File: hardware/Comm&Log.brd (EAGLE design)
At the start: 47 x 40.5 mm, 25 parts, among them J1 DM3AT-SF-PEJM5, U1 S25FL116K0XMFI043, U2 CAT24M01

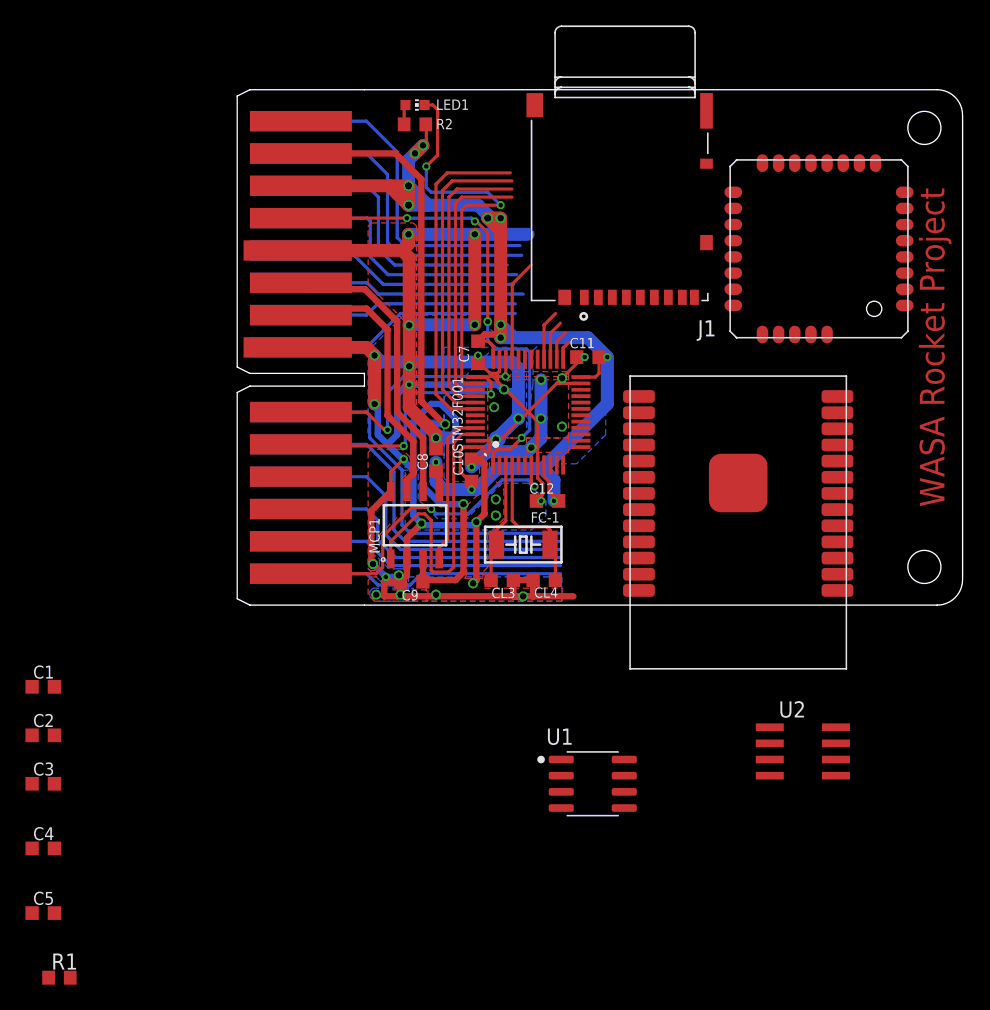
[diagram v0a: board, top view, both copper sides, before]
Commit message: Complete communication & logging board
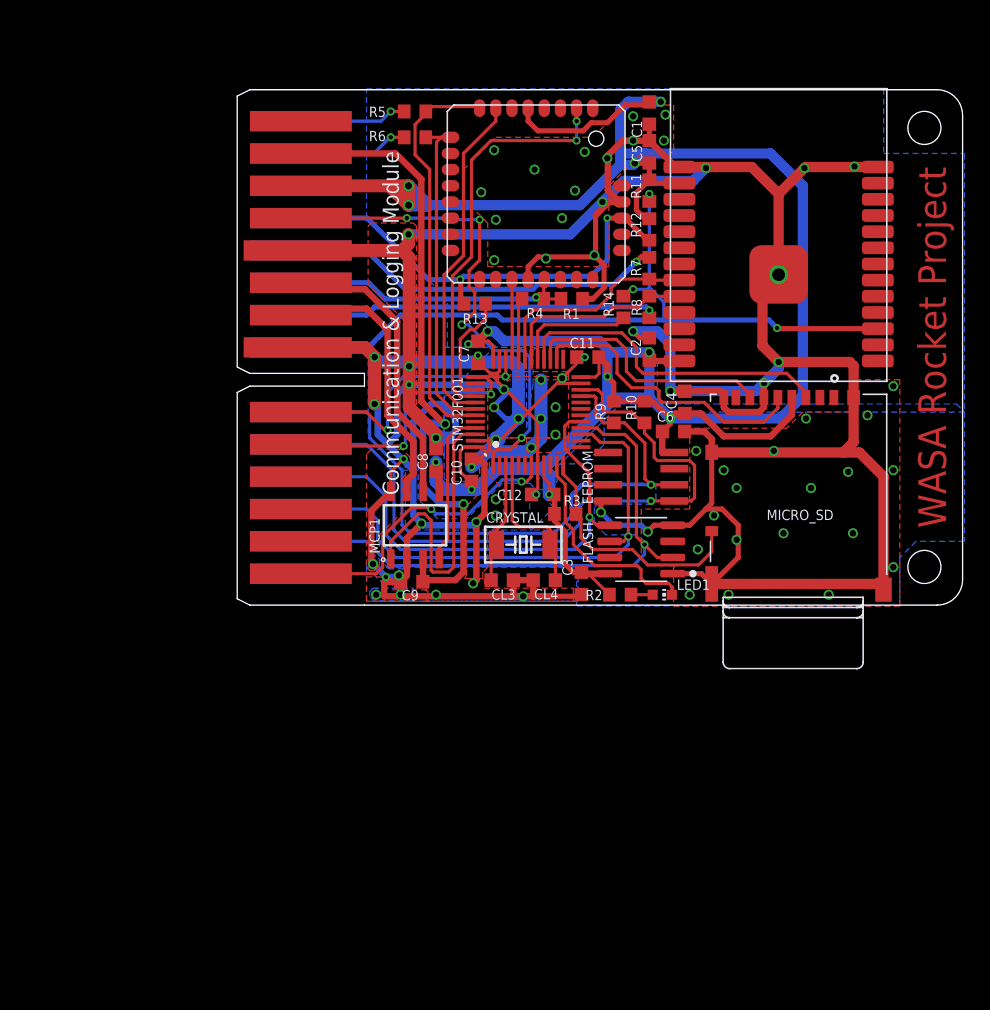
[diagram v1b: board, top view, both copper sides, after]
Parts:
- removed J1: DM3AT-SF-PEJM5, dm3at-sf-pejm5:HRS_DM3AT-SF-PEJM5
- removed U$1: ES920LR, FaBo-LoRa:ES920LR
- removed U$3: LITE, TWELite:LITE
- removed U1: S25FL116K0XMFI043, S25FL116K0XMFI043:SOIC127P600X175-8N
- removed U2: CAT24M01, CAT24M01:SO-8
- added C6: 0.1µF, rcl:C0603K
- added EEPROM: CAT24M01, CAT24M01:SO-8
- added ES920LR: ES920LR, FaBo-LoRa:ES920LR
- added FLASH: S25FL116K0XMFI043, S25FL116K0XMFI043:SOIC127P600X175-8N
- added MICRO_SD: DM3AT-SF-PEJM5, dm3at-sf-pejm5:HRS_DM3AT-SF-PEJM5
- added R10, R11, R12, R9: 10k, resistor:R0603
- added R13, R14: 1k, resistor:R0603
- added R3: 10k, rcl:R0603
- added R4, R5, R6, R7, R8: 1k, rcl:R0603
- added TWE-LITE: LITE, TWELite:LITE
- moved C5 76.5 mm to (32.4, 15.4), turned to 270 degrees
- moved R1 66.8 mm to (26.3, 3.81), turned to 180 degrees
- moved C1 65.6 mm to (32.4, 18.4), turned to 270 degrees
- moved C4 61.4 mm to (35.2, -4.32), turned to 90 degrees
- moved C2 56.5 mm to (32.4, -0.13), turned to 90 degrees
- moved C3 45.1 mm to (27.1, -18.5), turned to 270 degrees
- moved LED1 43.1 mm to (33.4, -19.4)
- moved R2 40.3 mm to (30.1, -19.4), turned to 0 degrees
- moved C12 0.63 mm to (24.0, -11.6)
- renumbered FC-1 to CRYSTAL
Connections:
- removed net 920_USART_RX: STM32F001.31, U$1.8
- removed net 920_USART_TX: STM32F001.30, U$1.9
- removed net I2C1_SCL: STM32F001.42, U2.6
- removed net I2C1_SDA: STM32F001.43, U2.5
- removed net N$33: U$2.30
- removed net N$34: U$2.29
- removed net N$35: U$2.28
- removed net N$36: U$2.27
- removed net N$43: U$2.26
- removed net N$44: U$2.25
- removed net N$45: U$2.23
- removed net N$46: U$2.22
- removed net N$47: U$2.21
- removed net N$48: U$2.20
- removed net N$49: U$2.19
- removed net N$50: U$2.18
- removed net N$56: STM32F001.15
- removed net N$57: STM32F001.16
- removed net N$58: STM32F001.17
- removed net N$61: STM32F001.33
- removed net N$65: STM32F001.21
- removed net N$66: J1.SWA, STM32F001.22
- removed net SPI1_MISO: J1.7, STM32F001.40
- removed net SPI1_MOSI: J1.3, STM32F001.41
- removed net SPI1_NSS: J1.2, STM32F001.38
- removed net SPI1_SCK: J1.5, STM32F001.39
- removed net SPI2_MISO: STM32F001.27, U1.2
- removed net SPI2_MOSI: STM32F001.28, U1.5
- removed net SPI2_NSS: STM32F001.25, U1.1
- removed net SPI2_SCK: STM32F001.26, U1.6
- removed net TWE_USART_RX: STM32F001.13, U$3.8
- removed net TWE_USART_TX: STM32F001.12, U$3.9
- new net 920_!SLEEP!': R14.1, STM32F001.29
- new net 920_RTX: ES920LR.8, R7.1, STM32F001.31
- new net 920_TRX: ES920LR.9, R8.1, STM32F001.30
- new net EEPROM_SCL: EEPROM.6, R9.1, STM32F001.21, U$2.25
- new net EEPROM_SDA: EEPROM.5, R10.1, STM32F001.22, U$2.26
- new net FLASH_MISO: FLASH.2, STM32F001.16, U$2.29
- new net FLASH_MOSI: FLASH.5, STM32F001.17, U$2.27
- new net FLASH_SCK: FLASH.6, STM32F001.15, U$2.28
- new net N$1: ES920LR.24
- new net N$3: R4.1, STM32F001.32
- new net N$4: R6.2, U$2.17
- new net N$5: R7.2, U$2.20
- new net N$6: R13.1, STM32F001.39
- new net SD_!SS!: MICRO_SD.2
- new net SD_!SW!: MICRO_SD.SWA, R3.2, STM32F001.12
- new net SD_MISO: MICRO_SD.7, STM32F001.27
- new net SD_MOSI: MICRO_SD.3, STM32F001.28
- new net SD_SCK: MICRO_SD.5, STM32F001.26
- new net TWE_BPS: STM32F001.33, TWE-LITE.19
- new net TWE_RTX: R5.1, STM32F001.43, TWE-LITE.8
- new net TWE_TRX: R6.1, STM32F001.42, TWE-LITE.9
- net 920_!SLEEP!: now also ES920LR.16, R11.1, R14.2, U$2.23; no longer U$1.16
- net GND: now also C6.2, EEPROM.4, ES920LR.1, ES920LR.26, ES920LR.GND, FLASH.1, FLASH.4, MICRO_SD.6, MICRO_SD.P1, MICRO_SD.P2, MICRO_SD.P3, MICRO_SD.P4, MICRO_SD.SWB, R1.1, TWE-LITE.20, TWE-LITE.28; no longer J1.6, J1.P1, J1.P2, J1.P3, J1.P4, J1.SWB, U$1.1, U$1.26, U$1.GND, U$3.20, U$3.28, U1.4, U2.4
- net N$2: now also R8.2, U$2.22; no longer U2.2
- net N$73: now also STM32F001.11
- net N$74: now also R5.2
- net TWE_!PGM!: now also STM32F001.40, TWE-LITE.2; no longer STM32F001.10, U$3.2
- net TWE_!RESET!: now also R1.2, R4.2, TWE-LITE.21, U$2.21; no longer R1.1, STM32F001.14, U$3.21
- net TWE_!RTS!: now also STM32F001.41, TWE-LITE.7; no longer STM32F001.11, U$3.7
- net TWE_SLEEP: now also R12.1, R13.2, TWE-LITE.27, U$2.19; no longer U$2.17, U$3.27
- net VDD: now also C6.1, EEPROM.8, ES920LR.13, ES920LR.2, FLASH.8, MICRO_SD.4, R10.2, R11.2, R12.2, R3.1, R9.2, TWE-LITE.5; no longer J1.4, R1.2, U$1.13, U$1.2, U$3.5, U1.8, U2.8
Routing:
- net GND: track 217.6 -> 396.7 mm, vias 35 -> 78
- net VDD: track 96.7 -> 214.9 mm
- net 920_!SLEEP!: track 0.00 -> 60.2 mm, vias 0 -> 3
- net EEPROM_SDA: track 0.00 -> 54.8 mm, vias 0 -> 1
- net EEPROM_SCL: track 0.00 -> 50.2 mm, vias 0 -> 1
- net FLASH_MISO: track 0.00 -> 44.5 mm, vias 0 -> 1
- net FLASH_SCK: track 0.00 -> 42.0 mm, vias 0 -> 1
- net FLASH_MOSI: track 0.00 -> 40.0 mm, vias 0 -> 1
- net TWE_!PGM!: track 0.00 -> 32.0 mm, vias 0 -> 2
- net TWE_RTX: track 0.00 -> 31.9 mm
- net N$5: track 0.00 -> 29.7 mm, vias 0 -> 1
- net N$2: track 0.00 -> 28.3 mm, vias 0 -> 1
- net N$44: track 27.8 -> 0.00 mm
- net TWE_!RTS!: track 0.00 -> 26.7 mm
- net TWE_TRX: track 0.00 -> 26.5 mm
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- added copper zone on layer 16, net VDD
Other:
- board text added: "Communication & Logging Module"
- board text added: "Designed by @fujiy0, 2019"

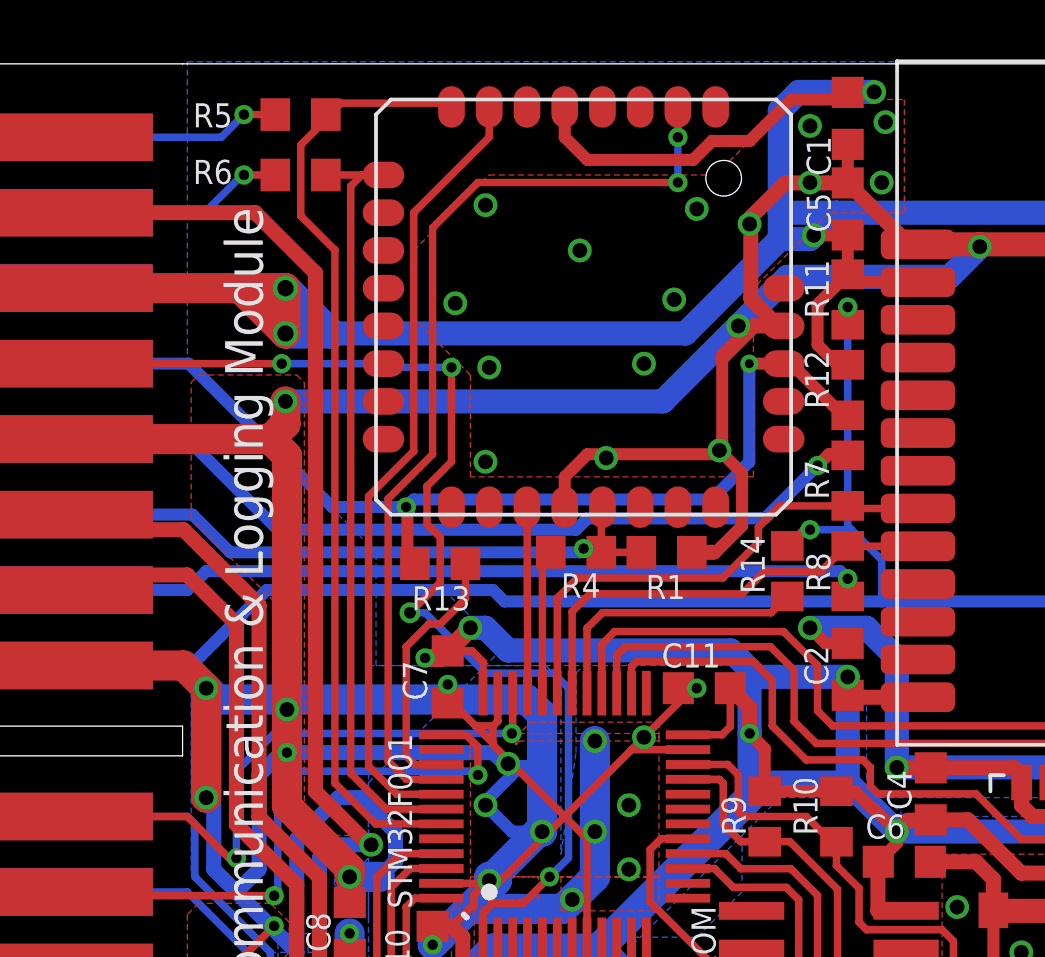
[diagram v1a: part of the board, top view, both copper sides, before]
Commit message: Clean silk print
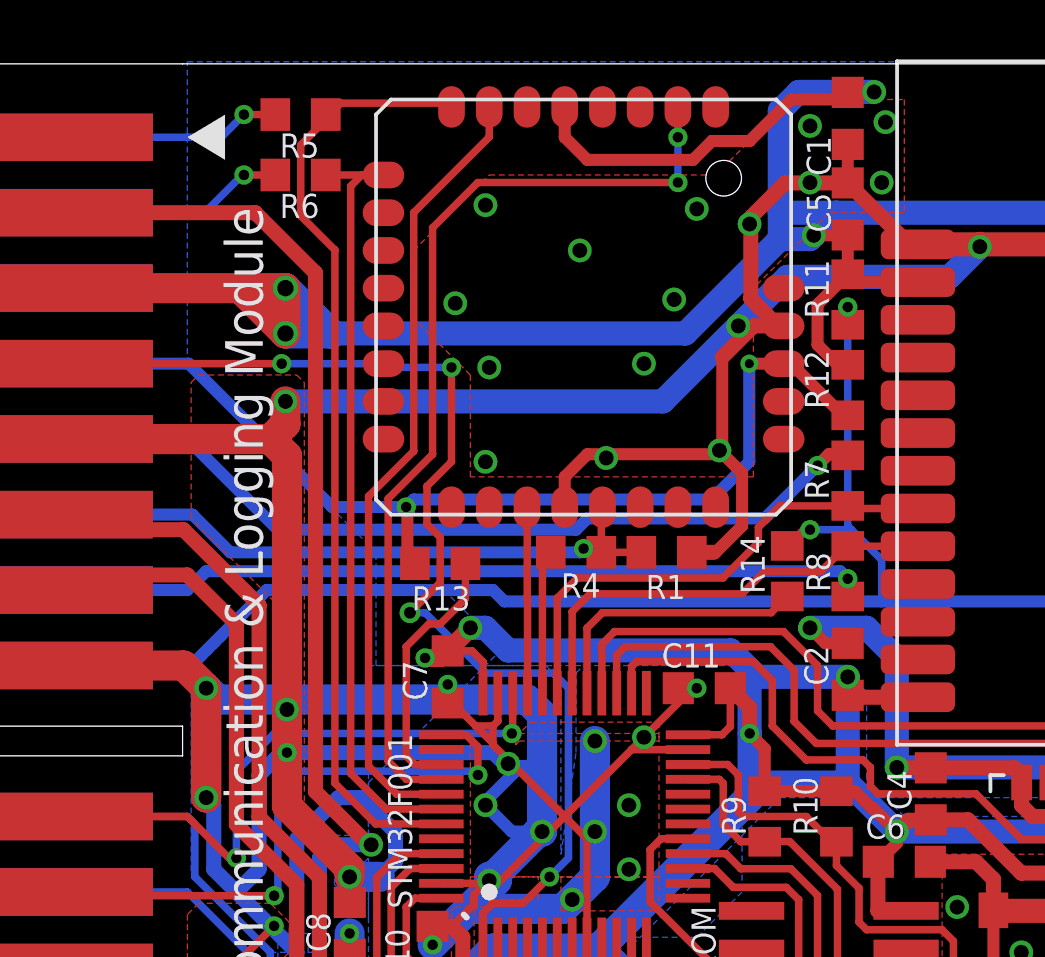
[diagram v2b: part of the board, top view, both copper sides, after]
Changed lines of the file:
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@@
 <layer number="27" name="tValues" color="7" fill="1" visible="no" active="yes"/>
 <layer number="28" name="bValues" color="7" fill="1" visible="no" active="yes"/>
-<layer number="29" name="tStop" color="7" fill="3" visible="no" active="yes"/>
+<layer number="29" name="tStop" color="7" fill="3" visible="yes" active="yes"/>
 <layer number="30" name="bStop" color="7" fill="6" visible="no" active="yes"/>
 <layer number="31" name="tCream" color="7" fill="4" visible="no" active="yes"/>
@@
 <text x="12.065" y="1.905" size="1.27" layer="25" font="vector" rot="R90" align="center">Communication &amp; Logging Module</text>
 <text x="55.88" y="-7.62" size="0.8128" layer="30" font="vector" rot="MR270" align="center">Designed by @fujiy0, 2019</text>
+<polygon width="0" layer="21">
+<vertex x="10.16" y="17.78"/>
+<vertex x="11.43" y="18.542"/>
+<vertex x="11.43" y="17.018"/>
+</polygon>
 </plain>
 <attributes>
@@
 </element>
 <element name="R5" library="rcl" library_urn="urn:adsk.eagle:library:334" package="R0603" package3d_urn="urn:adsk.eagle:package:23555/3" value="1k" x="13.97" y="18.542" smashed="yes" rot="R180">
-<attribute name="NAME" x="11.684" y="18.923" size="0.8128" layer="25" font="vector" rot="R180"/>
+<attribute name="NAME" x="14.605" y="17.907" size="0.8128" layer="25" font="vector" rot="R180"/>
 <attribute name="POPULARITY" value="77" x="13.97" y="18.542" size="1.778" layer="27" rot="R180" display="off"/>
 <attribute name="SPICEPREFIX" value="R" x="13.97" y="18.542" size="1.778" layer="27" rot="R180" display="off"/>
@@
 </element>
 <element name="R6" library="rcl" library_urn="urn:adsk.eagle:library:334" package="R0603" package3d_urn="urn:adsk.eagle:package:23555/3" value="1k" x="13.97" y="16.51" smashed="yes" rot="R180">
-<attribute name="NAME" x="11.684" y="17.018" size="0.8128" layer="25" font="vector" rot="R180"/>
+<attribute name="NAME" x="14.605" y="15.875" size="0.8128" layer="25" font="vector" rot="R180"/>
 <attribute name="POPULARITY" value="77" x="13.97" y="16.51" size="1.778" layer="27" rot="R180" display="off"/>
 <attribute name="SPICEPREFIX" value="R" x="13.97" y="16.51" size="1.778" layer="27" rot="R180" display="off"/>
@@
 <vertex x="34.29" y="-5.08"/>
 <vertex x="33.02" y="-3.81"/>
-<vertex x="33.02" y="-1.27"/>
-<vertex x="31.75" y="0"/>
+<vertex x="33.02" y="-0.889"/>
+<vertex x="32.131" y="0"/>
 <vertex x="16.51" y="0"/>
 <vertex x="16.51" y="3.81"/>

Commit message: Some fixes
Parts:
- C12: value (none) -> 0.1µF
- R2: value (none) -> 470
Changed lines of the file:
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@@
 <?xml version="1.0" encoding="utf-8"?>
 <!DOCTYPE eagle SYSTEM "eagle.dtd">
-<eagle version="9.5.1">
+<eagle version="9.5.2">
 <drawing>
 <settings>
@@
 <layer number="14" name="Route14" color="22" fill="1" visible="no" active="no"/>
 <layer number="15" name="Route15" color="23" fill="1" visible="no" active="no"/>
-<layer number="16" name="Bottom" color="1" fill="1" visible="yes" active="yes"/>
+<layer number="16" name="Bottom" color="1" fill="1" visible="no" active="yes"/>
 <layer number="17" name="Pads" color="2" fill="1" visible="yes" active="yes"/>
 <layer number="18" name="Vias" color="2" fill="1" visible="yes" active="yes"/>
@@
 <layer number="20" name="Dimension" color="24" fill="1" visible="yes" active="yes"/>
 <layer number="21" name="tPlace" color="7" fill="1" visible="yes" active="yes"/>
-<layer number="22" name="bPlace" color="7" fill="1" visible="yes" active="yes"/>
+<layer number="22" name="bPlace" color="7" fill="1" visible="no" active="yes"/>
 <layer number="23" name="tOrigins" color="15" fill="1" visible="yes" active="yes"/>
-<layer number="24" name="bOrigins" color="15" fill="1" visible="yes" active="yes"/>
+<layer number="24" name="bOrigins" color="15" fill="1" visible="no" active="yes"/>
 <layer number="25" name="tNames" color="7" fill="1" visible="yes" active="yes"/>
-<layer number="26" name="bNames" color="7" fill="1" visible="yes" active="yes"/>
+<layer number="26" name="bNames" color="7" fill="1" visible="no" active="yes"/>
 <layer number="27" name="tValues" color="7" fill="1" visible="no" active="yes"/>
 <layer number="28" name="bValues" color="7" fill="1" visible="no" active="yes"/>
-<layer number="29" name="tStop" color="7" fill="3" visible="yes" active="yes"/>
+<layer number="29" name="tStop" color="7" fill="3" visible="no" active="yes"/>
 <layer number="30" name="bStop" color="7" fill="6" visible="no" active="yes"/>
 <layer number="31" name="tCream" color="7" fill="4" visible="no" active="yes"/>
@@
 <layer number="38" name="bTest" color="7" fill="1" visible="no" active="yes"/>
 <layer number="39" name="tKeepout" color="4" fill="11" visible="yes" active="yes"/>
-<layer number="40" name="bKeepout" color="1" fill="11" visible="yes" active="yes"/>
+<layer number="40" name="bKeepout" color="1" fill="11" visible="no" active="yes"/>
 <layer number="41" name="tRestrict" color="4" fill="10" visible="yes" active="yes"/>
-<layer number="42" name="bRestrict" color="1" fill="10" visible="yes" active="yes"/>
+<layer number="42" name="bRestrict" color="1" fill="10" visible="no" active="yes"/>
 <layer number="43" name="vRestrict" color="2" fill="10" visible="no" active="yes"/>
 <layer number="44" name="Drills" color="7" fill="1" visible="no" active="yes"/>
@@
 <layer number="50" name="dxf" color="7" fill="1" visible="no" active="no"/>
 <layer number="51" name="tDocu" color="7" fill="1" visible="yes" active="yes"/>
-<layer number="52" name="bDocu" color="7" fill="1" visible="yes" active="yes"/>
+<layer number="52" name="bDocu" color="7" fill="1" visible="no" active="yes"/>
 <layer number="53" name="tGND_GNDA" color="7" fill="9" visible="no" active="no"/>
 <layer number="54" name="bGND_GNDA" color="1" fill="9" visible="no" active="no"/>
@@
 <attribute name="VALUE" x="28.359" y="0.888" size="1.016" layer="27" rot="R180"/>
 </element>
-<element name="C12" library="rcl" library_urn="urn:adsk.eagle:library:334" package="C0603K" package3d_urn="urn:adsk.eagle:package:23680/2" value="" x="24.003" y="-11.557" smashed="yes" rot="R180">
+<element name="C12" library="rcl" library_urn="urn:adsk.eagle:library:334" package="C0603K" package3d_urn="urn:adsk.eagle:package:23680/2" value="0.1µF" x="24.003" y="-11.557" smashed="yes" rot="R180">
 <attribute name="NAME" x="22.39" y="-11.191" size="0.8128" layer="25" font="vector" rot="R180"/>
 <attribute name="POPULARITY" value="30" x="24.003" y="-11.557" size="1.778" layer="27" rot="R180" display="off"/>
@@
 <attribute name="SPICEPREFIX" value="C" x="24.13" y="-18.288" size="1.778" layer="27" display="off"/>
 </element>
-<element name="R2" library="rcl" library_urn="urn:adsk.eagle:library:334" package="R0603" package3d_urn="urn:adsk.eagle:package:23555/3" value="" x="30.099" y="-19.431" smashed="yes">
+<element name="R2" library="rcl" library_urn="urn:adsk.eagle:library:334" package="R0603" package3d_urn="urn:adsk.eagle:package:23555/3" value="470" x="30.099" y="-19.431" smashed="yes">
 <attribute name="NAME" x="28.702" y="-19.05" size="0.8128" layer="25" font="vector" rot="R180"/>
 <attribute name="POPULARITY" value="77" x="30.099" y="-19.431" size="1.778" layer="27" display="off"/>
